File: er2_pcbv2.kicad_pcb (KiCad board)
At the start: 2 copper layers, 76.2 x 53.3 mm, 52 parts, among them IC1 LM2596S, IC2 L293DD, IC3 L293DD, P1 CONN_02X03, P2 CONN_02X03, P3 CONN_02X13, P4 CONN_01X05, P5 CONN_01X04, P6 CONN_01X02, P7 CONN_01X02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

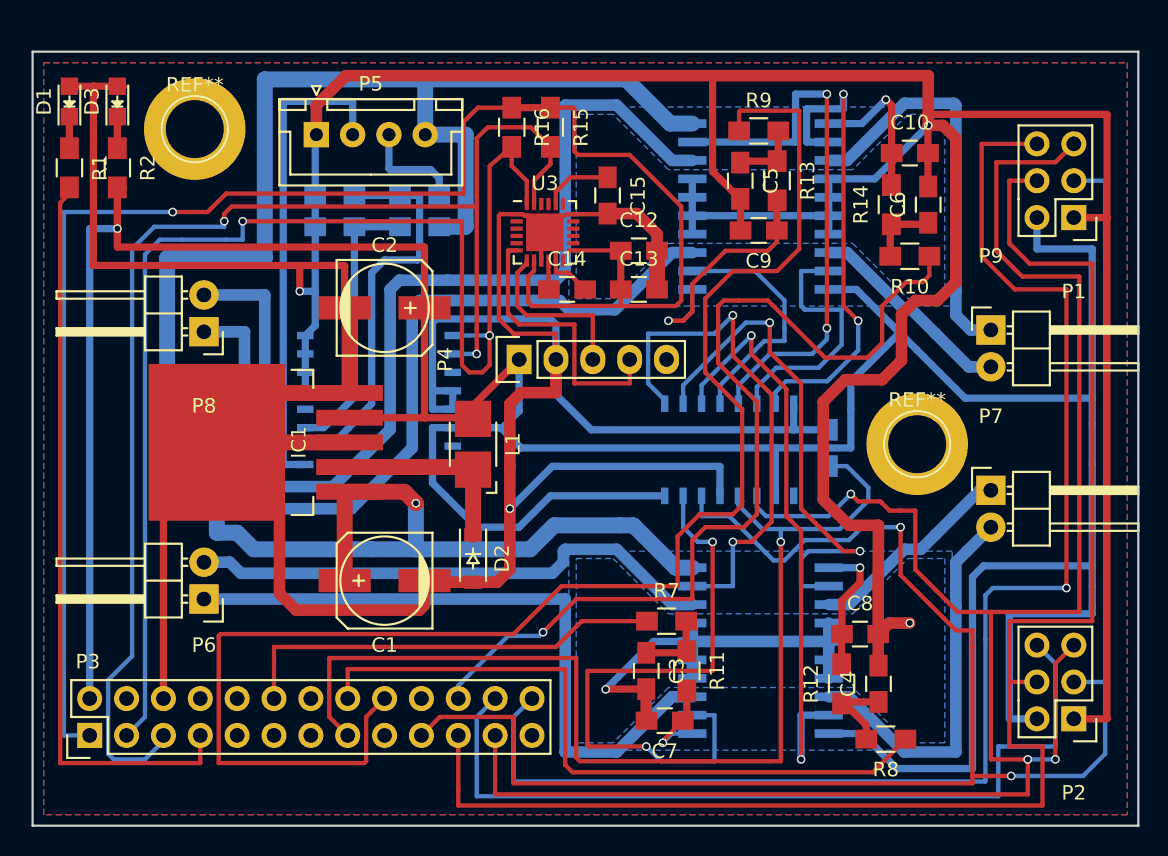
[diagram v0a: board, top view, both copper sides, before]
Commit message: power supply 12V connector added
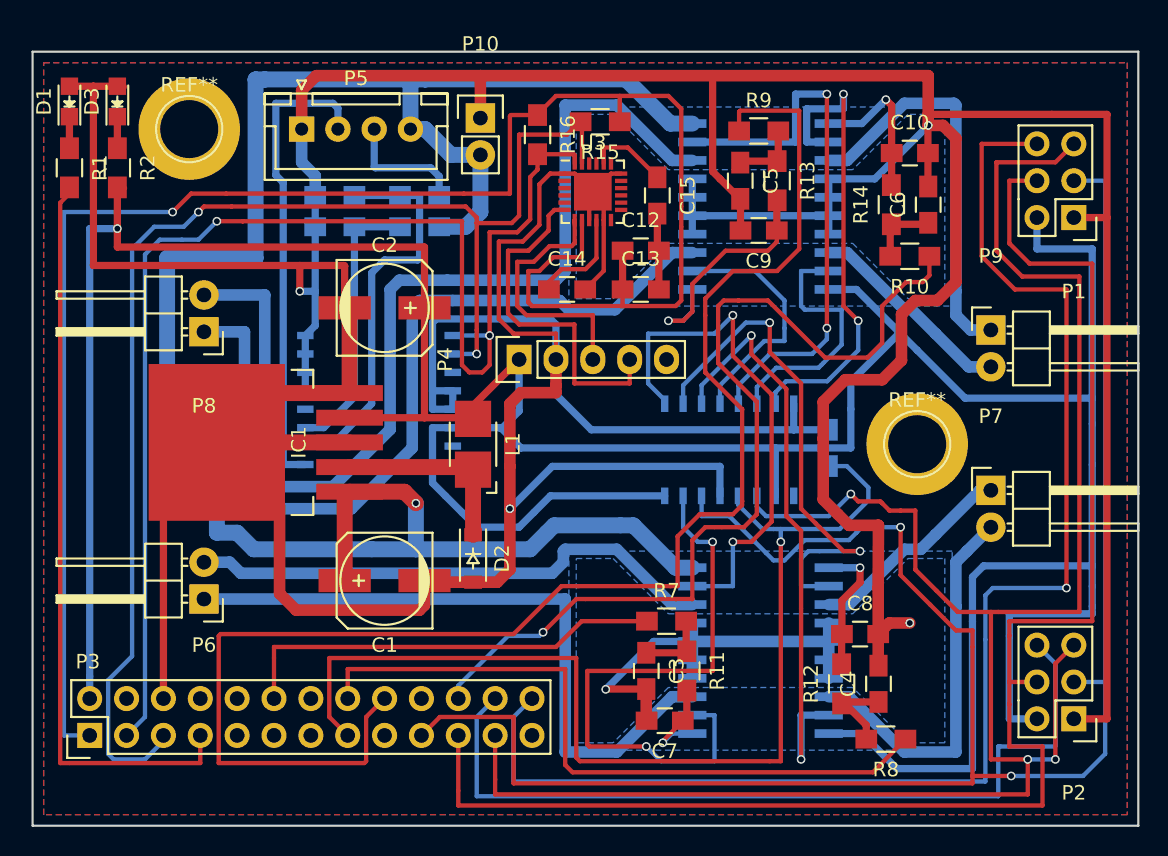
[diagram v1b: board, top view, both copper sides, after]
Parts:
- added P10: CONN_01X02, Pin_Headers:Pin_Header_Straight_1x02, F.Cu at (140.7, 78.9)
- moved U3 4.33 mm to (148.5, 83.9)
- moved R15 3.45 mm to (149.0, 79.1), turned to 180 degrees
- moved C15 3.43 mm to (152.9, 84.2)
- moved R16 1.85 mm to (144.7, 80.0)
- moved P5 1.09 mm to (128.4, 79.6)
- moved REF** 0.38 mm to (120.7, 79.6)
- moved C12 0.13 mm to (151.8, 88.0)
- moved C13 0.13 mm to (151.8, 90.7)
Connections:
- P3 pad 10: (no net) -> Net-(P3-Pad10)
- P3 pad 11: (no net) -> Net-(P3-Pad11)
- P3 pad 13: (no net) -> Net-(P3-Pad13)
- P3 pad 14: (no net) -> Net-(P3-Pad14)
- P3 pad 17: (no net) -> Net-(P3-Pad17)
- P3 pad 20: (no net) -> Net-(P3-Pad20)
- P3 pad 25: (no net) -> Net-(P3-Pad25)
- P3 pad 4: (no net) -> Net-(P3-Pad4)
- P3 pad 8: (no net) -> Net-(P3-Pad8)
- P3 pad 9: (no net) -> Net-(P3-Pad9)
- P4 pad 5: (no net) -> Net-(P4-Pad5)
- U1 pad 11: (no net) -> Net-(U1-Pad11)
- U1 pad 15: (no net) -> Net-(U1-Pad15)
- U1 pad 4: (no net) -> Net-(U1-Pad4)
- U2 pad 9: (no net) -> Net-(U2-Pad9)
- U3 pad 12: (no net) -> Net-(U3-Pad12)
- U3 pad 14: (no net) -> Net-(U3-Pad14)
- U3 pad 15: (no net) -> Net-(U3-Pad15)
- U3 pad 16: (no net) -> Net-(U3-Pad16)
- U3 pad 17: (no net) -> Net-(U3-Pad17)
- U3 pad 19: (no net) -> Net-(U3-Pad19)
- U3 pad 2: (no net) -> Net-(U3-Pad2)
- U3 pad 21: (no net) -> Net-(U3-Pad21)
- U3 pad 22: (no net) -> Net-(U3-Pad22)
- U3 pad 3: (no net) -> Net-(U3-Pad3)
- U3 pad 4: (no net) -> Net-(U3-Pad4)
- U3 pad 5: (no net) -> Net-(U3-Pad5)
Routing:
- net +3V3: track 118.2 -> 125.6 mm
- net GND: track 479.7 -> 487.0 mm
- net /mpu6050/AUX_CL: track 11.9 -> 17.9 mm
- net Net-(C14-Pad1): track 2.00 -> 7.11 mm
- net /mpu6050/AUX_DA: track 19.3 -> 24.4 mm
- net +12V: track 136.4 -> 137.8 mm
- net Net-(P5-Pad3): track 7.26 -> 8.66 mm
- net Net-(P5-Pad2): track 33.6 -> 32.5 mm
- net Net-(C15-Pad1): track 4.82 -> 5.65 mm

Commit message: pcb: silk placed exactly
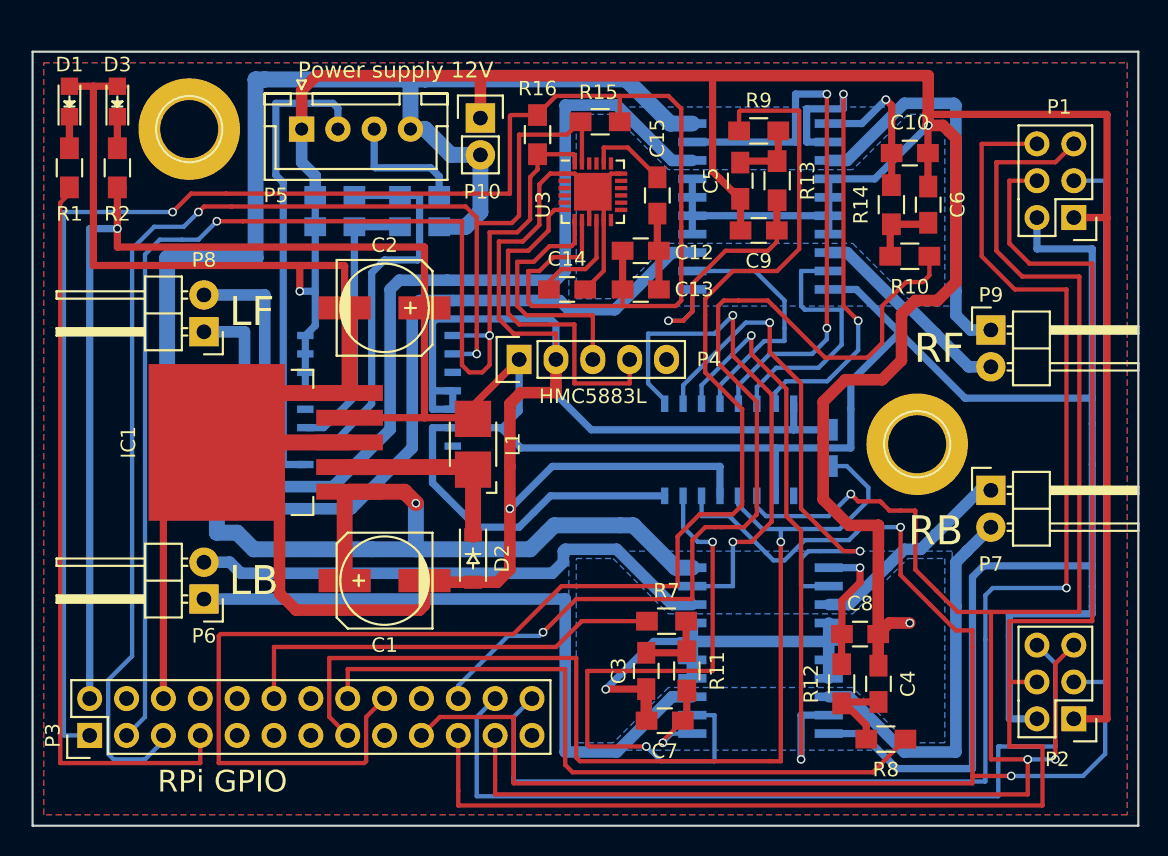
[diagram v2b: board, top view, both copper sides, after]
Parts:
- ?: renamed from REF**; value 1pin -> (none)
- renumbered REF** to ?
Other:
- board text added: "HMC5883L"
- board text added: "LB"
- board text added: "LF"
- board text added: "Power supply 12V"
- board text added: "RB"
- board text added: "RF"
- board text added: "RPi GPIO"

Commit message: pcb: label and logo silk added
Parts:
- added G***: LOGO, er2_pcb:logo, F.Cu at (149.4, 104.8)
- added G***: LOGO, er2_pcb:oh, F.Cu at (164.1, 106.9)
- ?: value 1pin -> (none)
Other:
- board text added: "er2_controller"
- board text added: "https://github.com/razykov/er_pcb"
- board text added: "v2(rev2)"

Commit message: pcb: SPI silk added
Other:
- board text added: "SPI1"
- board text added: "SPI2"
- board text added: "er2 controller"
- board text removed: "er2_controller"
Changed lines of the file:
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@@
-(kicad_pcb (version 4) (host pcbnew 4.0.3-stable)
+(kicad_pcb (version 4) (host pcbnew 4.0.4-stable)
   (general
-    (links 0)
+    (links 154)
     (no_connects 2)
-    (area 109.779999 74.209 186.770001 127.710001)
+    (area 109.779999 74.219999 186.130001 127.710001)
     (thickness 1.6)
-    (drawings 162)
+    (drawings 178)
     (tracks 870)
     (zones 0)
@@
   (page A4)
   (layers
-    (0 F.Cu signal)
-    (31 B.Cu signal)
+    (0 F.Cu signal hide)
+    (31 B.Cu signal hide)
     (32 B.Adhes user)
     (33 F.Adhes user)
     (34 B.Paste user)
     (35 F.Paste user)
-    (36 B.SilkS user)
+    (36 B.SilkS user hide)
     (37 F.SilkS user)
     (38 B.Mask user)
@@
     (mod_text_size 1 1)
     (mod_text_width 0.15)
-    (pad_size 1.3 1.3)
-    (pad_drill 0)
+    (pad_size 2.2 2.2)
+    (pad_drill 1.3)
     (pad_to_mask_clearance 0)
     (aux_axis_origin 0 0)
@@
     (tags "capacitor 0805")
     (attr smd)
-    (fp_text reference C6 (at 0 2.032 90) (layer F.SilkS)
-      (effects (font (size 1 1) (thickness 0.15)))
-    )
-    (fp_text value 1uF (at 0 3.302 90) (layer F.Fab)
+    (fp_text reference C6 (at -2.159 1.905 270) (layer F.SilkS)
+      (effects (font (size 1 1) (thickness 0.15)))
+    )
+    (fp_text value 1uF (at -4.318 1.905 90) (layer F.Fab)
       (effects (font (size 1 1) (thickness 0.15)))
     )
@@
     (tags "capacitor 0805")
     (attr smd)
-    (fp_text reference C7 (at 0 -2.1 180) (layer F.SilkS)
+    (fp_text reference C7 (at -1.524 -2.032 180) (layer F.SilkS)
       (effects (font (size 1 1) (thickness 0.15)))
     )
@@
     (tags "capacitor 0805")
     (attr smd)
-    (fp_text reference C10 (at 0 -2.1) (layer F.SilkS)
+    (fp_text reference C10 (at -0.889 -2.032) (layer F.SilkS)
       (effects (font (size 1 1) (thickness 0.15)))
     )
@@
     (descr "Through hole pin header")
     (tags "pin header")
-    (fp_text reference P1 (at 1.016 7.62 360) (layer F.SilkS)
+    (fp_text reference P1 (at -1.143 8.382 360) (layer F.SilkS)
       (effects (font (size 1 1) (thickness 0.15)))
     )
@@
     (pad 6 thru_hole oval (at 2.54 5.08 180) (size 1.7272 1.7272) (drill 1.016) (layers *.Cu *.Mask F.SilkS)
       (net 38 "Net-(P1-Pad6)"))
-    (model Pin_Headers.3dshapes/Pin_Header_Straight_2x03.wrl
-      (at (xyz 0.05 -0.1 0))
-      (scale (xyz 1 1 1))
-      (rotate (xyz 0 0 90))
-    )
   )
   (module Pin_Headers:Pin_Header_Straight_2x03 (layer F.Cu)
@@
     (descr "Through hole pin header")
     (tags "pin header")
-    (fp_text reference P2 (at 1.143 -2.794 180) (layer F.SilkS)
+    (fp_text reference P2 (at -1.27 -3.429 180) (layer F.SilkS)
       (effects (font (size 1 1) (thickness 0.15)))
     )
@@
     (pad 6 thru_hole oval (at 2.54 5.08 180) (size 1.7272 1.7272) (drill 1.016) (layers *.Cu *.Mask F.SilkS)
       (net 39 "Net-(P2-Pad6)"))
-    (model Pin_Headers.3dshapes/Pin_Header_Straight_2x03.wrl
-      (at (xyz 0.05 -0.1 0))
-      (scale (xyz 1 1 1))
-      (rotate (xyz 0 0 90))
-    )
   )
   (module Pin_Headers:Pin_Header_Straight_2x13 (layer F.Cu)
@@
     (descr "Through hole pin header")
     (tags "pin header")
-    (fp_text reference P7 (at 0 5.08) (layer F.SilkS)
-      (effects (font (size 1 1) (thickness 0.15)))
-    )
-    (fp_text value CONN_01X02 (at 4.826 -2.54) (layer F.Fab)
+    (fp_text reference P7 (at 0 -2.413) (layer F.SilkS)
+      (effects (font (size 1 1) (thickness 0.15)))
+    )
+    (fp_text value CONN_01X02 (at 6.223 -2.54) (layer F.Fab)
       (effects (font (size 1 1) (thickness 0.15)))
     )
@@
     (descr "Through hole pin header")
     (tags "pin header")
-    (fp_text reference P9 (at 0 -2.413 180) (layer F.SilkS)
-      (effects (font (size 1 1) (thickness 0.15)))
-    )
-    (fp_text value CONN_01X02 (at 4.699 5.08) (layer F.Fab)
+    (fp_text reference P9 (at 0 5.08 180) (layer F.SilkS)
+      (effects (font (size 1 1) (thickness 0.15)))
+    )
+    (fp_text value CONN_01X02 (at 6.223 5.08) (layer F.Fab)
       (effects (font (size 1 1) (thickness 0.15)))
     )
@@
     (fp_line (start -1.27 1.27) (end -1.27 3.81) (layer F.SilkS) (width 0.15))
     (fp_line (start -1.27 3.81) (end 1.27 3.81) (layer F.SilkS) (width 0.15))
-    (pad 1 thru_hole rect (at 0 0) (size 2.032 2.032) (drill 1.016) (layers *.Cu *.Mask F.SilkS)
-      (net 2 GND))
-    (pad 2 thru_hole oval (at 0 2.54) (size 2.032 2.032) (drill 1.016) (layers *.Cu *.Mask F.SilkS)
+    (pad 1 thru_hole rect (at 0 0) (size 2.2 2.2) (drill 1.3) (layers *.Cu *.Mask F.SilkS)
+      (net 2 GND))
+    (pad 2 thru_hole circle (at 0 2.54) (size 2.2 2.2) (drill 1.3) (layers *.Cu *.Mask F.SilkS)
       (net 1 +12V))
-    (model Pin_Headers.3dshapes/Pin_Header_Straight_1x02.wrl
-      (at (xyz 0 -0.05 0))
-      (scale (xyz 1 1 1))
-      (rotate (xyz 0 0 90))
-    )
   )
   (module er2_pcb:logo (layer F.Cu)
@@
       (xy 0.006706 -2.1971) (xy 0.011179 -2.197101) (xy 0.116093 -2.196689)) (layer F.SilkS) (width 0.01))
   )
+  (gr_text SPI2 (at 174.498 83.185 90) (layer F.SilkS)
+    (effects (font (size 1.5 1.5) (thickness 0.3)))
+  )
+  (gr_text SPI1 (at 174.498 117.729 90) (layer F.SilkS)
+    (effects (font (size 1.5 1.5) (thickness 0.3)))
+  )
+  (gr_line (start 175.895 110.109) (end 184.912 110.109) (angle 90) (layer F.SilkS) (width 0.2))
+  (gr_line (start 184.912 110.109) (end 184.912 125.349) (angle 90) (layer F.SilkS) (width 0.2))
+  (gr_line (start 184.912 125.349) (end 175.895 125.349) (angle 90) (layer F.SilkS) (width 0.2))
+  (gr_line (start 175.895 125.349) (end 175.895 110.109) (angle 90) (layer F.SilkS) (width 0.2))
+  (gr_line (start 183.388 115.697) (end 184.912 115.697) (angle 90) (layer F.SilkS) (width 0.2))
+  (gr_line (start 183.388 115.697) (end 183.388 119.761) (angle 90) (layer F.SilkS) (width 0.2))
+  (gr_line (start 183.388 119.761) (end 184.912 119.761) (angle 90) (layer F.SilkS) (width 0.2))
+  (gr_line (start 183.388 85.217) (end 184.912 85.217) (angle 90) (layer F.SilkS) (width 0.2))
+  (gr_line (start 183.388 81.153) (end 183.388 85.217) (angle 90) (layer F.SilkS) (width 0.2))
+  (gr_line (start 183.388 81.153) (end 184.912 81.153) (angle 90) (layer F.SilkS) (width 0.2))
+  (gr_line (start 175.895 90.805) (end 175.895 75.565) (angle 90) (layer F.SilkS) (width 0.2))
+  (gr_line (start 184.912 90.805) (end 175.895 90.805) (angle 90) (layer F.SilkS) (width 0.2))
+  (gr_line (start 184.912 75.565) (end 184.912 90.805) (angle 90) (layer F.SilkS) (width 0.2))
+  (gr_line (start 175.895 75.565) (end 184.912 75.565) (angle 90) (layer F.SilkS) (width 0.2))
   (gr_text https://github.com/razykov/er_pcb (at 112.903 99.949 90) (layer B.SilkS)
     (effects (font (size 1.1 1.1) (thickness 0.25)) (justify mirror))
@@
     (effects (font (size 1.3 1.3) (thickness 0.26)))
   )
-  (gr_text er2_controller (at 159.639 100.965) (layer F.SilkS)
+  (gr_text "er2 controller" (at 159.639 100.965) (layer F.SilkS)
     (effects (font (size 1.3 1.3) (thickness 0.26)))
   )

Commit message: pcb: silk small changes
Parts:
- added G***: LOGO, er2_pcb:octocat, B.Cu at (114.0, 81.8)

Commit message: pcb: tracing optimization
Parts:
- moved G*** 6.87 mm to (157.4, 108.3)
- moved R8 6.23 mm to (162.4, 121.3)
- moved R12 4.57 mm to (161.0, 117.9)
- moved C8 4.57 mm to (162.3, 114.4)
- moved C4 4.44 mm to (163.7, 117.9)
- moved U2 2.41 mm to (155.4, 101.7)
- moved ? 2.34 mm to (168.5, 101.9)
- moved C3 2.29 mm to (149.9, 116.8)
- moved C11 2.29 mm to (162.4, 101.6)
- moved R11 2.29 mm to (152.7, 117.0)
- moved R7 2.29 mm to (151.3, 113.5)
- moved C7 2.16 mm to (151.3, 120.4)
- moved C15 2.03 mm to (152.9, 82.2)
- moved C6 1.65 mm to (169.9, 84.8)
- moved P7 1.65 mm to (174.2, 104.5)
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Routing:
- net /DC-motors drivers/RCLK: track 75.3 -> 50.1 mm, vias 1 -> 3
- net Net-(IC2-Pad2): track 41.2 -> 21.4 mm
- net +5V: track 256.7 -> 237.9 mm
- net Net-(IC2-Pad9): track 36.1 -> 20.5 mm
- net Net-(IC2-Pad12): track 36.1 -> 23.8 mm
- net Net-(P1-Pad4): track 104.8 -> 94.6 mm
- net /DC-motors drivers/pwm4: track 65.7 -> 56.4 mm
- net Net-(P1-Pad6): track 96.3 -> 88.4 mm
- net /DC-motors drivers/SER: track 134.4 -> 127.0 mm
- net /DC-motors drivers/pwm2: track 48.2 -> 42.2 mm
- net /DC-motors drivers/pwm3: track 103.8 -> 98.5 mm
- net GND: track 487.0 -> 491.9 mm
- net Net-(IC3-Pad19): track 17.8 -> 13.9 mm
- net +3V3: track 125.6 -> 129.0 mm
- net /DC-motors drivers/pwm3_f: track 17.2 -> 13.8 mm
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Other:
- board size 76.2 x 53.3 mm -> 76.2 x 52.6 mm
